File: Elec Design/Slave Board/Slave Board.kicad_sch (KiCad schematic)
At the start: 100 parts, among them J1 JTAG, J2 OSTTC020162, J3 OSTTC030162, J4 OSTTC020162, J5 OSTTC030162, J6 0022232041, J8 OSTTC020162, J9 OSTTC020162, M1 VID28-05, M2 VID28-05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

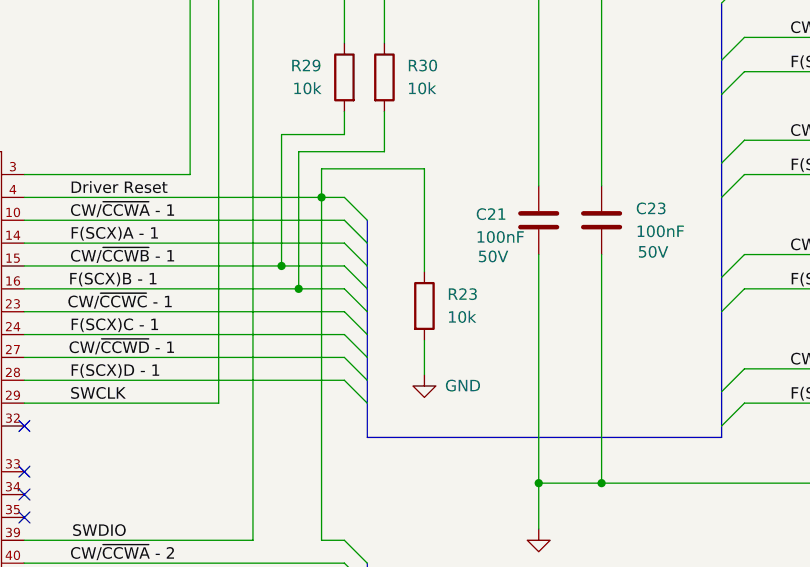
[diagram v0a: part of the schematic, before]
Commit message: removed driver reset pulldown resistor
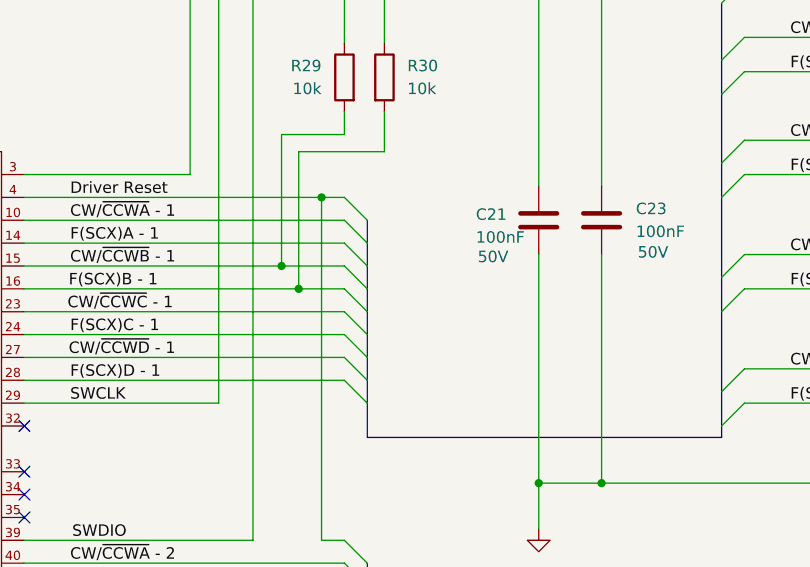
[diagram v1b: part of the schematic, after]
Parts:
- removed R23: 10k, Resistor_SMD:R_0805_2012Metric_Pad1.20x1.40mm_HandSolder, symbol Device:R
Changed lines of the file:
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@@
     (stroke (width 0) (type default))
   )
-  (wire (pts (xy 226.06 183.515) (xy 237.49 183.515))
-    (stroke (width 0) (type default))
-  )
   (wire (pts (xy 147.32 152.4) (xy 166.37 152.4))
     (stroke (width 0) (type default))
@@
     (stroke (width 0) (type default))
   )
-  (wire (pts (xy 226.06 183.515) (xy 226.06 186.69))
-    (stroke (width 0) (type default))
-  )
   (wire (pts (xy 182.88 -52.07) (xy 186.69 -52.07))
     (stroke (width 0) (type default))
@@
     (stroke (width 0) (type default))
   )
-  (wire (pts (xy 237.49 202.565) (xy 237.49 206.375))
-    (stroke (width 0) (type default))
-  )
   (wire (pts (xy 347.98 204.47) (xy 351.79 204.47))
     (stroke (width 0) (type default))
@@
     (stroke (width 0) (type default))
   )
-  (wire (pts (xy 237.49 183.515) (xy 237.49 194.945))
-    (stroke (width 0) (type default))
-  )
   (wire (pts (xy 218.44 139.7) (xy 218.44 224.79))
     (stroke (width 0) (type default))
@@
     )
   )
-  (symbol (lib_id "Device:R") (at 237.49 198.755 0) (unit 1)
-    (in_bom yes) (on_board yes) (dnp no) (fields_autoplaced)
-    (property "Reference" "R23" (at 240.03 197.4849 0)
-      (effects (font (size 1.27 1.27)) (justify left))
-    )
-    (property "Value" "10k" (at 240.03 200.0249 0)
-      (effects (font (size 1.27 1.27)) (justify left))
-    )
-    (property "Footprint" "Resistor_SMD:R_0805_2012Metric_Pad1.20x1.40mm_HandSolder" (at 235.712 198.755 90)
-      (effects (font (size 1.27 1.27)) hide)
-    )
-    (property "Datasheet" "https://www.digikey.ca/en/htmldatasheets/production/781422/0/0/1/rmcf0805ft20m0.html?site=CA&lang=en&cur=CAD" (at 237.49 198.755 0)
-      (effects (font (size 1.27 1.27)) hide)
-    )
-    (property "DK_Datasheet_Link" "https://www.digikey.ca/en/htmldatasheets/production/781422/0/0/1/rmcf0805ft20m0.html?site=CA&lang=en&cur=CAD" (at 237.49 198.755 0)
-      (effects (font (size 1.27 1.27)) hide)
-    )
-    (property "DK_Detail_Page" "https://www.digikey.ca/en/products/detail/stackpole-electronics-inc/RMCF0805FT10K0/1760676" (at 237.49 198.755 0)
-      (effects (font (size 1.27 1.27)) hide)
-    )
-    (pin "1")
-    (pin "2")
-    (instances
-      (project "Slave Board"
-        (path "/1d9bb2ee-6cce-4dc6-9479-bffa6635df30"
-          (reference "R23") (unit 1)
-        )
-      )
-    )
-  )
   (symbol (lib_id "Device:C") (at 86.36 240.03 0) (unit 1)
     (in_bom yes) (on_board yes) (dnp no)
@@
         )
       )
-    )
-  )
-  (symbol (lib_id "power:GND") (at 237.49 206.375 0) (unit 1)
-    (in_bom yes) (on_board yes) (dnp no) (fields_autoplaced)
-    (property "Reference" "#PWR011" (at 237.49 212.725 0)
-      (effects (font (size 1.27 1.27)) hide)
-    )
-    (property "Value" "GND" (at 239.776 207.6449 0)
-      (effects (font (size 1.27 1.27)) (justify left))
-    )
-    (property "Footprint" "" (at 237.49 206.375 0)
-      (effects (font (size 1.27 1.27)) hide)
-    )
-    (property "Datasheet" "" (at 237.49 206.375 0)
-      (effects (font (size 1.27 1.27)) hide)
-    )
-    (pin "1")
-    (instances
-      (project "Slave Board"
-        (path "/1d9bb2ee-6cce-4dc6-9479-bffa6635df30"
-          (reference "#PWR011") (unit 1)
-        )
-      )

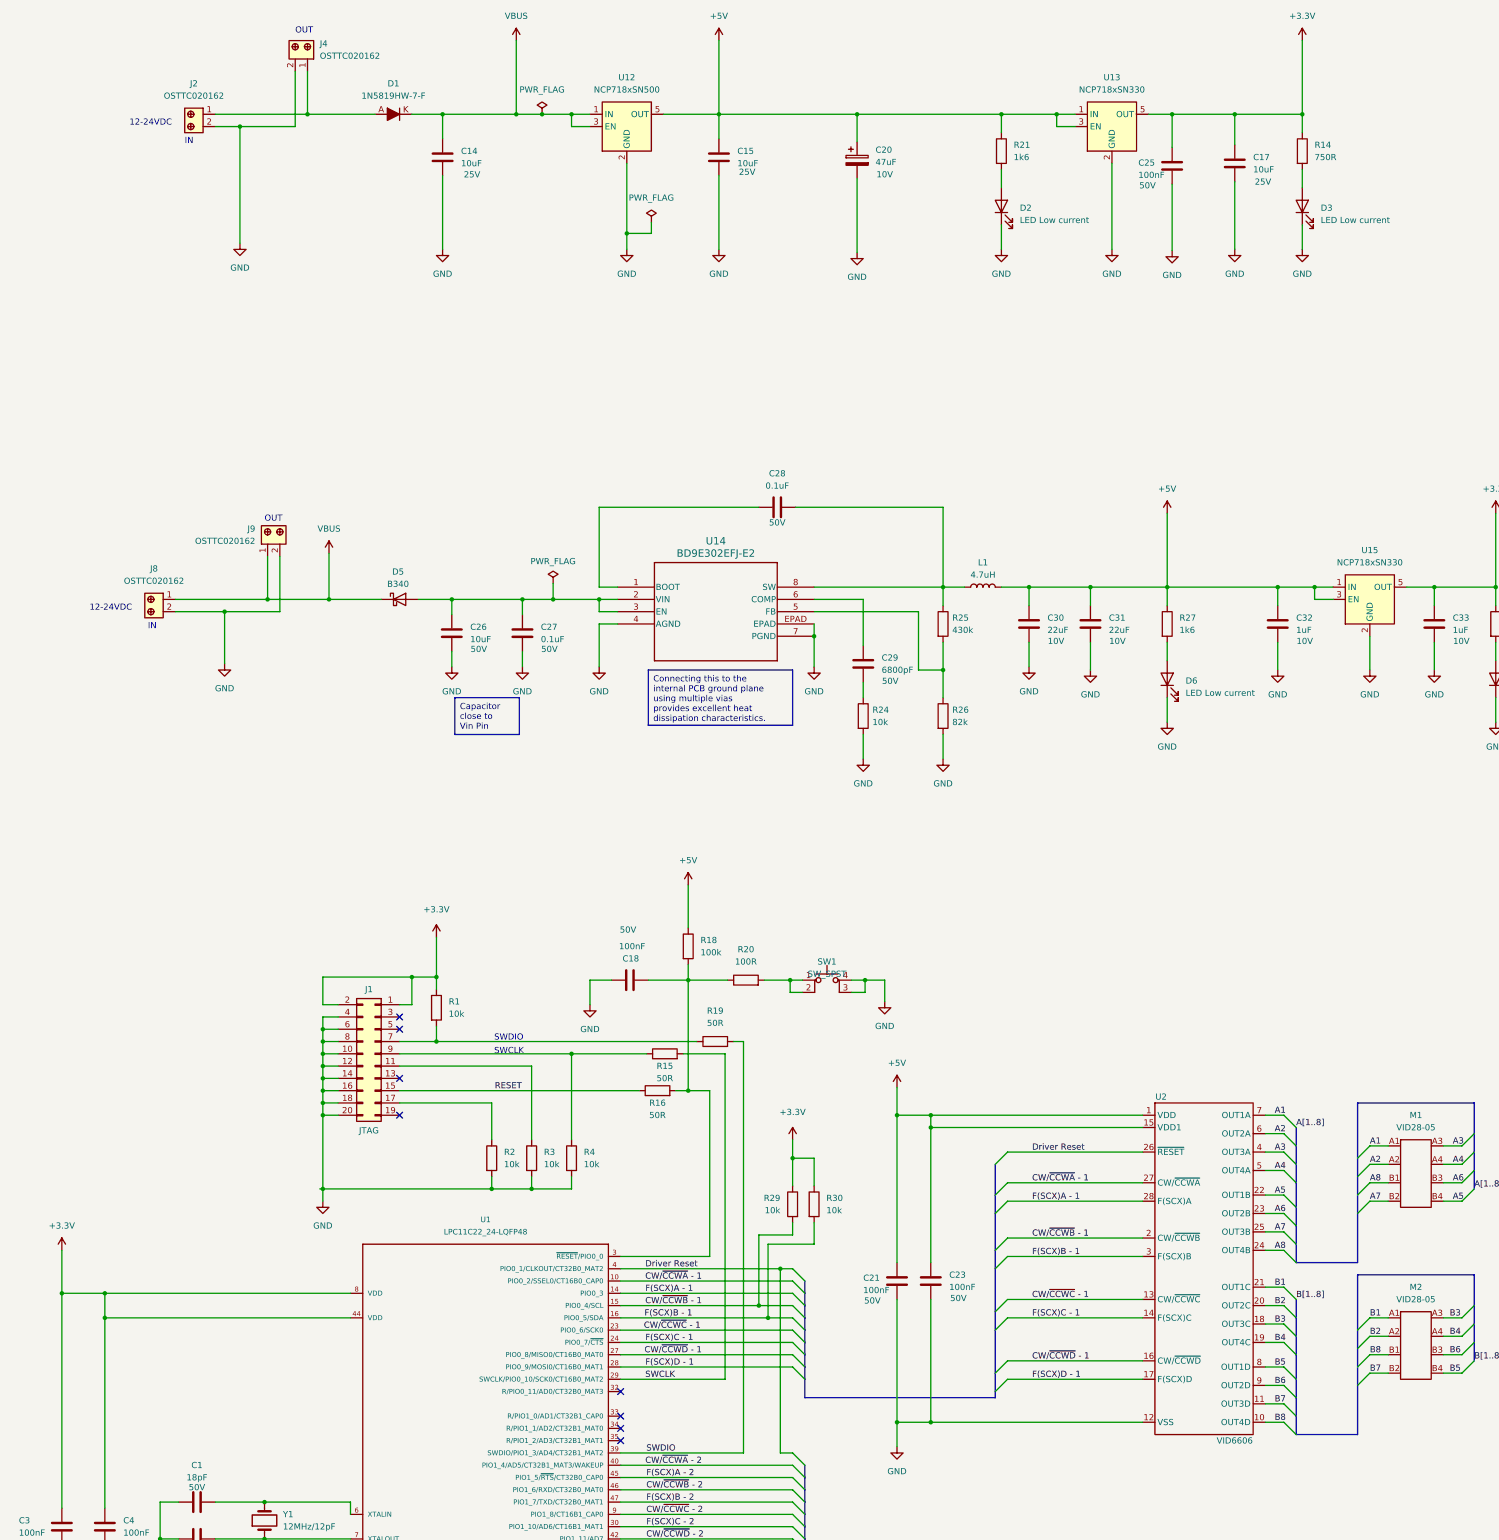
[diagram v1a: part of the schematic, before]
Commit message: slave board changes. changed jtag port and power supply
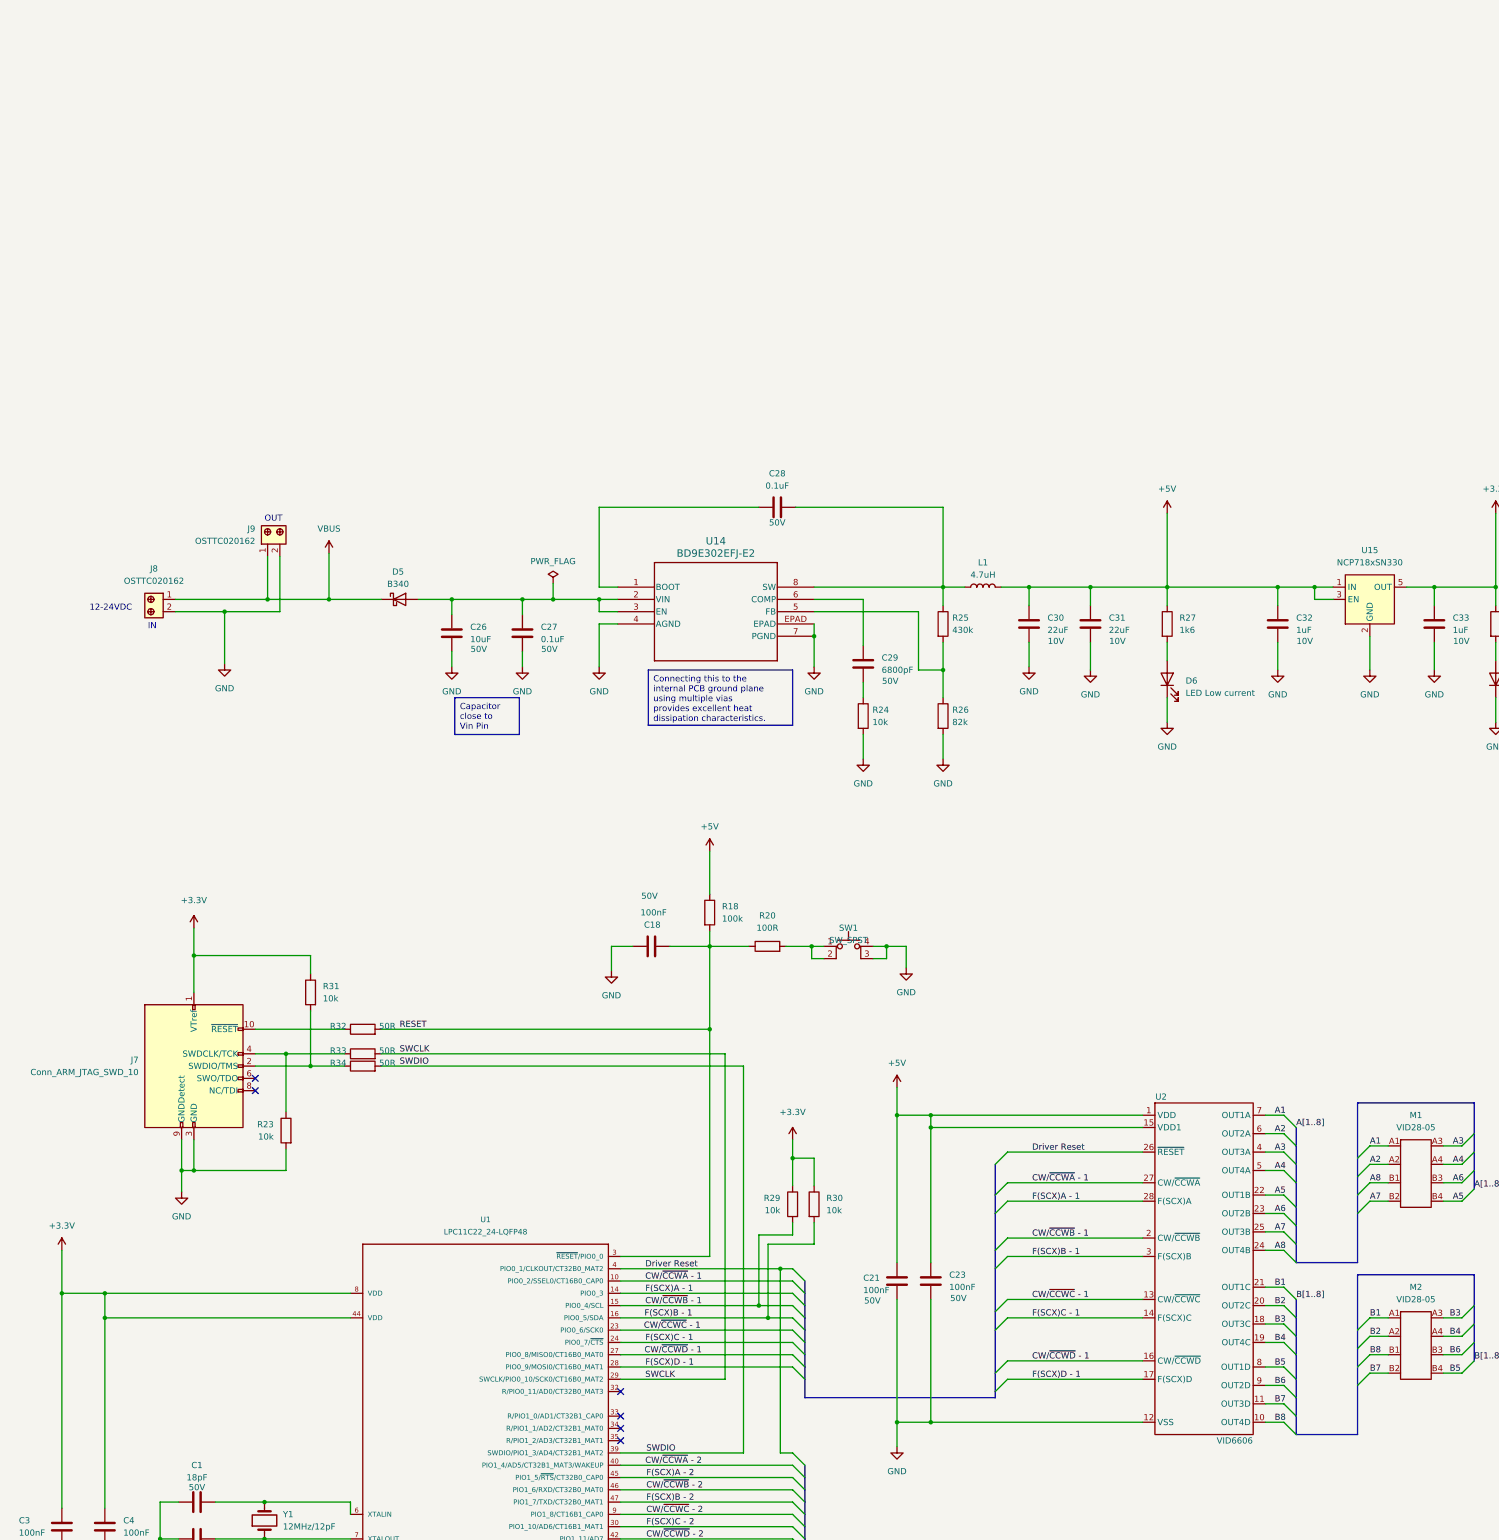
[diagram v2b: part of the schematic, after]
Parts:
- removed C14, C15, C17: 10uF, Capacitor_SMD:C_1206_3216Metric_Pad1.33x1.80mm_HandSolder, symbol Device:C
- removed C20: 47uF, Capacitor_THT:CP_Radial_D6.3mm_P2.50mm, symbol Device:C_Polarized
- removed C25: 100nF, Capacitor_SMD:C_0805_2012Metric_Pad1.18x1.45mm_HandSolder, symbol Device:C
- removed D1: 1N5819HW-7-F, digikey-footprints:SOD-123, symbol dk_Diodes-Rectifiers-Single:1N5819HW-7-F
- removed D2, D3: LED Low current, LED_SMD:LED_0603_1608Metric, symbol Device:LED
- removed J1: JTAG, Connector_PinHeader_2.54mm:PinHeader_2x10_P2.54mm_Vertical, symbol Connector_Generic:Conn_02x10_Odd_Even
- removed J2, J4: OSTTC020162, digikey-footprints:Term_Block_1x2_P5mm, symbol dk_Terminal-Blocks-Wire-to-Board:OSTTC020162
- removed R1, R2, R3, R4: 10k, Resistor_SMD:R_0805_2012Metric_Pad1.20x1.40mm_HandSolder, symbol Device:R
- removed R14: 750R, Resistor_SMD:R_1206_3216Metric_Pad1.30x1.75mm_HandSolder, symbol Device:R
- removed R15, R16, R19: 50R, Resistor_SMD:R_0805_2012Metric_Pad1.20x1.40mm_HandSolder, symbol Device:R
- removed R21: 1k6, Resistor_SMD:R_1206_3216Metric_Pad1.30x1.75mm_HandSolder, symbol Device:R
- removed U12: NCP718xSN500, Package_TO_SOT_SMD:SOT-23-5, symbol Regulator_Linear:NCP718xSN500
- removed U13: NCP718xSN330, Package_TO_SOT_SMD:SOT-23-5, symbol Regulator_Linear:NCP718xSN330
- added J7: Conn_ARM_JTAG_SWD_10, 10 pin jtag:CONN_3220-10-0100-00_CNC, symbol Connector:Conn_ARM_JTAG_SWD_10
- added R23, R31: 10k, Resistor_SMD:R_0603_1608Metric, symbol Device:R
- added R32, R33, R34: 50R, Resistor_SMD:R_0603_1608Metric, symbol Device:R
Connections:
- net +3.3V: now also J7.1 (VTref), R31.1
- net GND: now also J7.3 (GND), J7.5 (GND), J7.9 (GNDDetect), R23.2
- net RESET: now also C18.2, R18.2, R20.1, U1.3 (~{RESET}/PIO0_0), R32.2
- net SWCLK : now also R33.2
- net SWDIO: now also R34.2
- new net: J7.2 (SWDIO/TMS), R31.2, R34.1
- new net: J7.4 (SWDCLK/TCK), R23.1, R33.1
- new net: J7.10 (~{RESET}), R32.1
- no-connect marks 11 -> 9
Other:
- note removed: "SWCLK"
- note removed: "SWDIO"
- moved on the sheet: C18, R18, R20, SW1

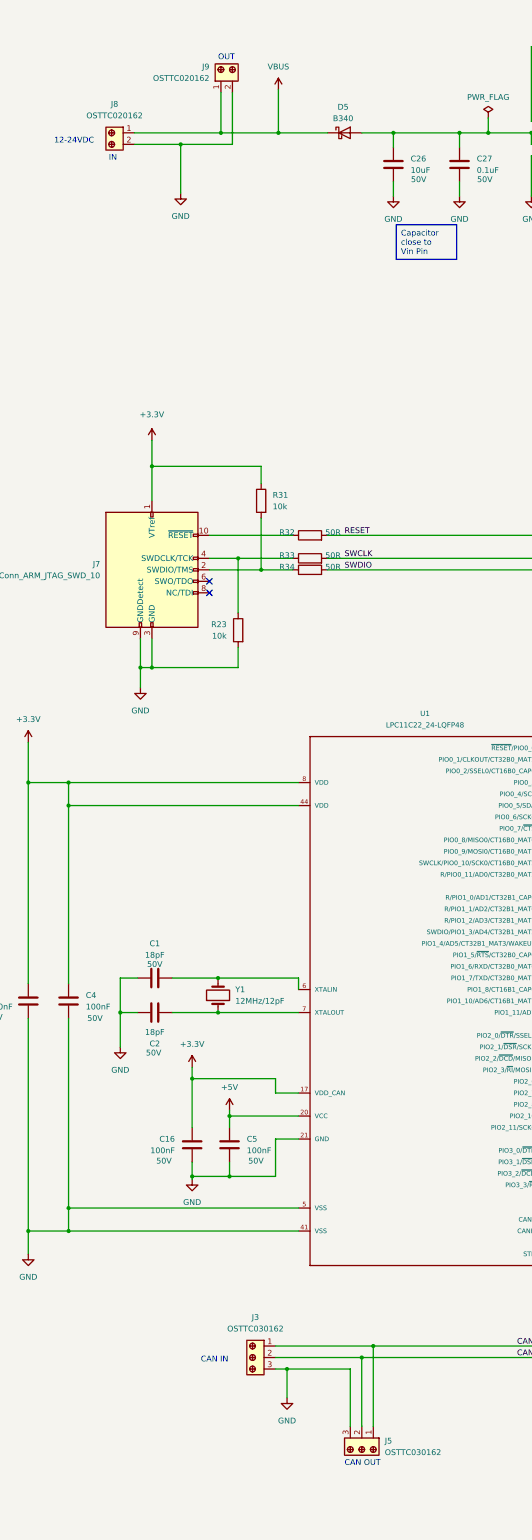
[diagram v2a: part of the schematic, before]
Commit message: lining up with JLC parts
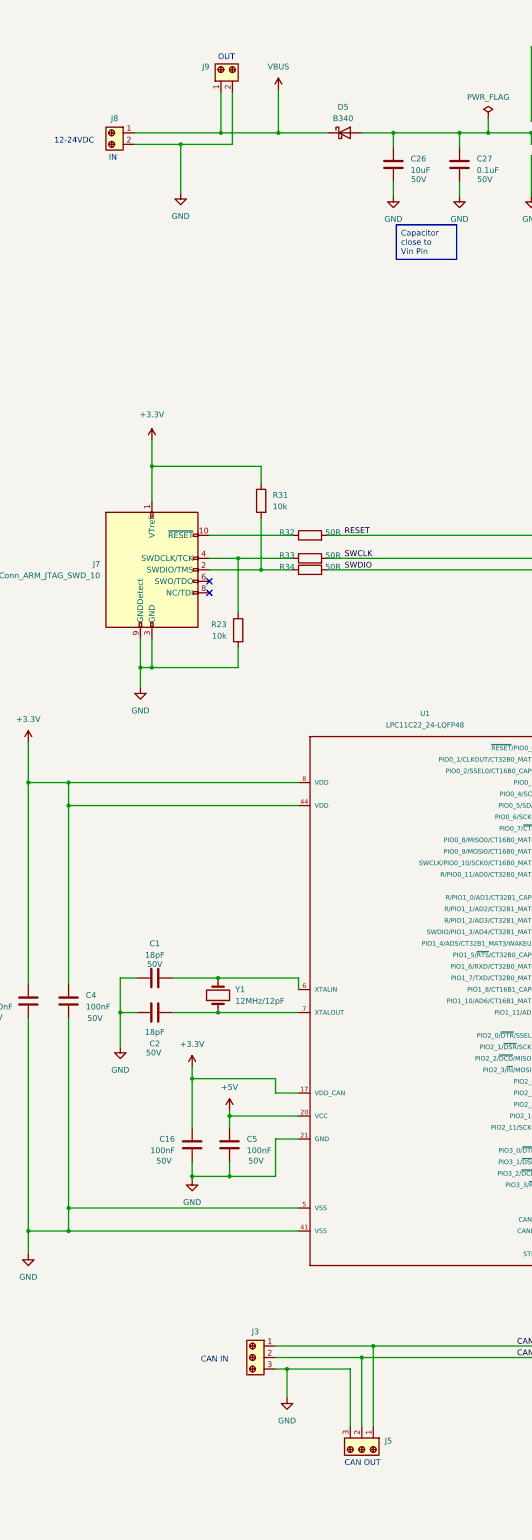
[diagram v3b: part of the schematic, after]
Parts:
- J3, J5: value OSTTC030162 -> ~; DK_Datasheet_Link http://www.on-shore.com/wp-content/uploads/OSTTCXX0162.pdf -> (none); DK_Detail_Page /product-detail/en/on-shore-technology-inc/OSTTC030162/ED26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 -> https://www.digikey.ca/en/products/detail/phoenix-contact/1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; Digi-Key_PN ED2601-ND -> 277-1578-ND; MPN OSTTC030162 -> 1935174; Manufacturer On Shore Technology Inc. -> Phoenix Contact
- J8, J9: value OSTTC020162 -> ~; footprint digikey-footprints:Term_Block_1x2_P5mm -> digikey-footprints:Terminal_Block_D1.3mm_P5mm; symbol dk_Terminal-Blocks-Wire-to-Board:OSTTC020162 -> dk_Terminal-Blocks-Wire-to-Board:1935161; DK_Datasheet_Link http://www.on-shore.com/wp-content/uploads/OSTTCXX0162.pdf -> https://media.digikey.com/pdf/Data%20Sheets/Phoenix%20Conta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; DK_Detail_Page /product-detail/en/on-shore-technology-inc/OSTTC020162/ED26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 -> /product-detail/en/phoenix-contact/1935161/277-1667-ND/5686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; Digi-Key_PN ED2600-ND -> 277-1667-ND; MPN OSTTC020162 -> 1935161; Manufacturer On Shore Technology Inc. -> Phoenix Contact
- SW1: footprint digikey-footprints:Switch_Tactile_SMD_6x6mm_PTS645 -> Switches:SW_SPST_ SKRPASE010; DK_Detail_Page https://www.digikey.ca/en/products/detail/c-k/PTS645SL50SMT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 -> https://jlcpcb.com/partdetail/Alpsalpine-SKRPASE010/C470427

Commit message: further JLC alignment
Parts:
- U1: value LPC11C22_24-LQFP48 -> LPC11C24-LQFP48
